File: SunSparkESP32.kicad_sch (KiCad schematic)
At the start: 51 parts, among them J1 Conn_01x02_Pin, J2 USB_C_Receptacle_USB2.0, J3 Conn_01x03_Pin, J4 Conn_01x15_Pin, J5 Conn_01x03_Pin, J6 Conn_01x15_Pin, J7 Conn_01x01_Pin, Q1 IRLML6244TRPBF, Q2 IRLML6244TRPBF, SW1 SW_Push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

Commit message: Rework due to first review -Replaced electrolytic caps with low ESR ceramic ones -Routing optimizations Also added possible connection for backup battery Routed some DIOs from LoRa module on controller Updated outputs and BOM
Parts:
- removed C2, C5: 4.7µ, Capacitor_SMD:CP_Elec_4x3, symbol Device:C_Polarized
- added C2, C5: 4µ7, Capacitor_SMD:C_0805_2012Metric_Pad1.18x1.45mm_HandSolder, symbol Device:C
- added J8: Conn_01x01_Pin, TestPoint:TestPoint_THTPad_D1.5mm_Drill0.7mm, symbol Connector:Conn_01x01_Pin
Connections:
- net GND: now also C2.2, C5.2
- net DIO3: now reaches U4.11 (DIO3)
- net DIO3: now also U3.33 (GPIO37)
- net DIO2: now reaches U4.16 (DIO2)
- net DIO2: now also U3.34 (GPIO38)
- net at J1.1 (Pin_1), L1.1, R2.1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: now also C5.1
- net at JP1.1 (A), TP3.1, U1.11 (SYS): now also C2.1
- net at U1.12 (BACKUP): now also J8.1 (Pin_1)
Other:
- note added: "DIO2/3 used for potential PreambleDetect/SyncAddress"
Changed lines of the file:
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@@
     (stroke (width 0) (type default))
   )
+  (wire (pts (xy 68.58 87.63) (xy 73.66 87.63))
+    (stroke (width 0) (type default))
+  )
   (wire (pts (xy 285.75 163.83) (xy 290.83 163.83))
     (stroke (width 0) (type default))
@@
     (stroke (width 0) (type default))
   )
+  (wire (pts (xy 361.95 116.84) (xy 361.95 113.03))
+    (stroke (width 0) (type default))
+  )
   (wire (pts (xy 212.09 153.67) (xy 212.09 154.94))
     (stroke (width 0) (type default))
@@
     (stroke (width 0) (type default))
   )
+  (wire (pts (xy 360.68 115.57) (xy 355.6 115.57))
+    (stroke (width 0) (type default))
+  )
   (wire (pts (xy 369.57 46.99) (xy 372.11 46.99))
     (stroke (width 0) (type default))
@@
     (stroke (width 0) (type default))
   )
+  (wire (pts (xy 360.68 120.65) (xy 364.49 120.65))
+    (stroke (width 0) (type default))
+  )
   (wire (pts (xy 281.94 41.91) (xy 289.56 41.91))
     (stroke (width 0) (type default))
@@
     (stroke (width 0) (type default))
   )
-  (bus (pts (xy 363.22 119.38) (xy 363.22 113.03))
+  (bus (pts (xy 363.22 113.03) (xy 363.22 110.49))
     (stroke (width 0) (type default))
   )
@@
     (stroke (width 0) (type default))
   )
-  (bus (pts (xy 363.22 110.49) (xy 363.22 113.03))
-    (stroke (width 0) (type default))
-  )
   (wire (pts (xy 129.54 87.63) (xy 129.54 95.25))
     (stroke (width 0) (type default))
@@
     (stroke (width 0) (type default))
   )
+  (wire (pts (xy 361.95 116.84) (xy 364.49 116.84))
+    (stroke (width 0) (type default))
+  )
   (wire (pts (xy 342.9 165.1) (xy 350.52 165.1))
     (stroke (width 0) (type default))
@@
     (stroke (width 0) (type default))
   )
+  (wire (pts (xy 361.95 113.03) (xy 355.6 113.03))
+    (stroke (width 0) (type default))
+  )
   (wire (pts (xy 100.33 39.37) (xy 100.33 43.18))
     (stroke (width 0) (type default))
@@
     (stroke (width 0) (type default))
   )
+  (wire (pts (xy 360.68 120.65) (xy 360.68 115.57))
+    (stroke (width 0) (type default))
+  )
   (wire (pts (xy 281.94 57.15) (xy 289.56 57.15))
     (stroke (width 0) (type default))
@@
     (stroke (width 0) (type default))
   )
+  (wire (pts (xy 236.22 201.93) (xy 242.57 201.93))
+    (stroke (width 0) (type default))
+  )
   (wire (pts (xy 355.6 87.63) (xy 356.87 87.63))
     (stroke (width 0) (type default))
@@
     (stroke (width 0) (type default))
   )
-  (bus (pts (xy 363.22 119.38) (xy 367.03 119.38))
+  (bus (pts (xy 363.22 113.03) (xy 367.03 113.03))
     (stroke (width 0) (type default))
   )
@@
     (stroke (width 0) (type default))
   )
+  (wire (pts (xy 236.22 204.47) (xy 242.57 204.47))
+    (stroke (width 0) (type default))
+  )
   (wire (pts (xy 302.26 166.37) (xy 302.26 163.83))
     (stroke (width 0) (type default))
@@
     (effects (font (size 1.27 1.27)) (justify left bottom))
   )
+  (text "DIO2/3 used for potential\nPreambleDetect/SyncAddress"
+    (at 241.3 199.39 0)
+    (effects (font (size 1.27 1.27)) (justify left bottom))
+  )
   (text "Might also be used to\ninsert shunt for\ncurrent meas."
     (at 78.74 31.75 0)
@@
     (effects (font (size 1.27 1.27)) (justify left bottom))
   )
-  (label "IO[0..4]" (at 367.03 119.38 0) (fields_autoplaced)
+  (label "IO[0..4]" (at 367.03 113.03 0) (fields_autoplaced)
     (effects (font (size 1.27 1.27)) (justify left bottom))
   )
@@
     )
   )
+  (global_label "DIO3" (shape input) (at 242.57 201.93 0) (fields_autoplaced)
+    (effects (font (size 1.27 1.27)) (justify left))
+    (property "Intersheetrefs" "${INTERSHEET_REFS}" (at 249.8906 201.93 0)
+      (effects (font (size 1.27 1.27)) (justify left) hide)
+    )
+  )
   (global_label "AUX_SW_CTRL" (shape input) (at 356.87 80.01 0) (fields_autoplaced)
     (effects (font (size 1.27 1.27)) (justify left))
@@
     )
   )
+  (global_label "DIO2" (shape input) (at 364.49 120.65 0) (fields_autoplaced)
+    (effects (font (size 1.27 1.27)) (justify left))
+    (property "Intersheetrefs" "${INTERSHEET_REFS}" (at 371.8106 120.65 0)
+      (effects (font (size 1.27 1.27)) (justify left) hide)
+    )
+  )
   (global_label "CS0" (shape input) (at 382.27 82.55 180) (fields_autoplaced)
     (effects (font (size 1.27 1.27)) (justify right))
@@
     )
   )
+  (global_label "DIO3" (shape input) (at 364.49 116.84 0) (fields_autoplaced)
+    (effects (font (size 1.27 1.27)) (justify left))
+    (property "Intersheetrefs" "${INTERSHEET_REFS}" (at 371.8106 116.84 0)
+      (effects (font (size 1.27 1.27)) (justify left) hide)
+    )
+  )
+  (global_label "DIO2" (shape input) (at 242.57 204.47 0) (fields_autoplaced)
+    (effects (font (size 1.27 1.27)) (justify left))
+    (property "Intersheetrefs" "${INTERSHEET_REFS}" (at 249.8906 204.47 0)
+      (effects (font (size 1.27 1.27)) (justify left) hide)
+    )
+  )
   (global_label "rst_btn" (shape input) (at 278.13 41.91 180) (fields_autoplaced)
     (effects (font (size 1.27 1.27)) (justify right))
@@
     )
   )
+  (symbol (lib_id "Device:C") (at 78.74 59.69 0) (unit 1)
+    (in_bom yes) (on_board yes) (dnp no) (fields_autoplaced)
+    (property "Reference" "C5" (at 82.55 59.055 0)
+      (effects (font (size 1.27 1.27)) (justify left))
+    )
+    (property "Value" "4µ7" (at 82.55 61.595 0)
+      (effects (font (size 1.27 1.27)) (justify left))
+    )
+    (property "Footprint" "Capacitor_SMD:C_0805_2012Metric_Pad1.18x1.45mm_HandSolder" (at 79.7052 63.5 0)
+      (effects (font (size 1.27 1.27)) hide)
+    )
+    (property "Datasheet" "~" (at 78.74 59.69 0)
+      (effects (font (size 1.27 1.27)) hide)
+    )
+    (pin "1")
+    (pin "2")
+    (instances
+      (project "SunSparkESP32"
+        (path "/d10941bc-74a1-4d19-894b-f93374d839a2"
+          (reference "C5") (unit 1)
+        )
+      )
+    )
+  )
   (symbol (lib_id "Device:C") (at 212.09 149.86 0) (unit 1)
     (in_bom yes) (on_board yes) (dnp no) (fields_autoplaced)
@@
     )
   )
-  (symbol (lib_id "Device:C_Polarized") (at 119.38 80.01 0) (unit 1)
-    (in_bom yes) (on_board yes) (dnp no)
-    (property "Reference" "C5" (at 121.92 80.01 0)
-      (effects (font (size 1.27 1.27)) (justify left))
-    )
-    (property "Value" "4.7µ" (at 120.65 82.55 0)
-      (effects (font (size 1.27 1.27)) (justify left))
-    )
-    (property "Footprint" "Capacitor_SMD:CP_Elec_4x3" (at 120.3452 83.82 0)
-      (effects (font (size 1.27 1.27)) hide)
-    )
-    (property "Datasheet" "~" (at 119.38 80.01 0)
-      (effects (font (size 1.27 1.27)) hide)
-    )
-    (pin "1")
-    (pin "2")
-    (instances
-      (project "SunSparkESP32"
-        (path "/d10941bc-74a1-4d19-894b-f93374d839a2"
-          (reference "C5") (unit 1)
-        )
-      )
-    )
-  )
   (symbol (lib_id "Device:R") (at 85.09 149.86 90) (unit 1)
     (in_bom yes) (on_board yes) (dnp no)
@@
     )
   )
-  (symbol (lib_id "power:+BATT") (at 260.35 34.29 0) (unit 1)
+  (symbol (lib_id "Device:C") (at 119.38 80.01 0) (unit 1)
     (in_bom yes) (on_board yes) (dnp no) (fields_autoplaced)
-    (property "Reference" "#PWR022" (at 260.35 38.1 0)
-      (effects (font (size 1.27 1.27)) hide)
+    (property "Reference" "C2" (at 123.19 79.375 0)
+      (effects (font (size 1.27 1.27)) (justify left))
     )
-    (property "Value" "+BATT" (at 260.35 30.48 0)
-      (effects (font (size 1.27 1.27)))
+    (property "Value" "4µ7" (at 123.19 81.915 0)
+      (effects (font (size 1.27 1.27)) (justify left))
     )
-    (property "Footprint" "" (at 260.35 34.29 0)
+    (property "Footprint" "Capacitor_SMD:C_0805_2012Metric_Pad1.18x1.45mm_HandSolder" (at 120.3452 83.82 0)
       (effects (font (size 1.27 1.27)) hide)
     )
-    (property "Datasheet" "" (at 260.35 34.29 0)
+    (property "Datasheet" "~" (at 119.38 80.01 0)
       (effects (font (size 1.27 1.27)) hide)
     )
     (pin "1")
+    (pin "2")
     (instances
       (project "SunSparkESP32"
         (path "/d10941bc-74a1-4d19-894b-f93374d839a2"
-          (reference "#PWR022") (unit 1)
+          (reference "C2") (unit 1)
         )
       )
     )
   )
-  (symbol (lib_id "Device:C_Polarized") (at 78.74 59.69 0) (unit 1)
-    (in_bom yes) (on_board yes) (dnp no)
-    (property "Reference" "C2" (at 81.28 59.69 0)
-      (effects (font (size 1.27 1.27)) (justify left))
+  (symbol (lib_id "power:+BATT") (at 260.35 34.29 0) (unit 1)
+    (in_bom yes) (on_board yes) (dnp no) (fields_autoplaced)
+    (property "Reference" "#PWR022" (at 260.35 38.1 0)
+      (effects (font (size 1.27 1.27)) hide)
     )
-    (property "Value" "4.7µ" (at 80.01 62.23 0)
-      (effects (font (size 1.27 1.27)) (justify left))
+    (property "Value" "+BATT" (at 260.35 30.48 0)
+      (effects (font (size 1.27 1.27)))
     )
-    (property "Footprint" "Capacitor_SMD:CP_Elec_4x3" (at 79.7052 63.5 0)
+    (property "Footprint" "" (at 260.35 34.29 0)
       (effects (font (size 1.27 1.27)) hide)
     )
-    (property "Datasheet" "~" (at 78.74 59.69 0)
+    (property "Datasheet" "" (at 260.35 34.29 0)
       (effects (font (size 1.27 1.27)) hide)
     )
     (pin "1")
-    (pin "2")
     (instances
       (project "SunSparkESP32"
         (path "/d10941bc-74a1-4d19-894b-f93374d839a2"
-          (reference "C2") (unit 1)
+          (reference "#PWR022") (unit 1)
         )
       )
@@
         )
       )
+    )
+  )
+  (symbol (lib_id "Connector:Conn_01x01_Pin") (at 63.5 87.63 0) (unit 1)
+    (in_bom yes) (on_board yes) (dnp no) (fields_autoplaced)
+    (property "Reference" "J8" (at 64.135 83.82 0)
+      (effects (font (size 1.27 1.27)))
+    )
+    (property "Value" "Conn_01x01_Pin" (at 64.135 86.36 0)
+      (effects (font (size 1.27 1.27)))
+    )
+    (property "Footprint" "TestPoint:TestPoint_THTPad_D1.5mm_Drill0.7mm" (at 63.5 87.63 0)
+      (effects (font (size 1.27 1.27)) hide)
+    )
+    (property "Datasheet" "~" (at 63.5 87.63 0)
+      (effects (font (size 1.27 1.27)) hide)
+    )
+    (pin "1")
+    (instances
+      (project "SunSparkESP32"
+        (path "/d10941bc-74a1-4d19-894b-f93374d839a2"
+          (reference "J8") (unit 1)
+        )
+      )

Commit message: Finalized last review points, enhanced doc -Added Diode to prevent discharge from supercap into LDO -Updated BOM -Made readme nicer
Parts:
- added D1: D_Schottky, Diode_SMD:D_SOD-323, symbol Device:D_Schottky
- added JP2: SolderJumper_2_Open, Jumper:SolderJumper-2_P1.3mm_Open_RoundedPad1.0x1.5mm, symbol Jumper:SolderJumper_2_Open
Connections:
- net at C6.1, U2.2 (VO): now also D1.2 (A), JP2.1 (A); no longer R14.1
- net BCKP: now reaches J8.1 (Pin_1), U1.12 (BACKUP)
- net BCKP: now also JP2.2 (B)
- new net: D1.1 (K), R14.1
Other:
- note added: "Prevent Supercap from discharging through LDO"
- moved on the sheet: J8, R1, R14, R2

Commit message: Added Routing for DIO pins of modem
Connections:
- net DIO4: now reaches U4.12 (DIO4)
- net DIO4: now also J6.13 (Pin_13), U3.7 (GPIO3/ADC1_CH2)
- net DIO0: now reaches U4.14 (DIO0)
- net DIO0: now also J6.14 (Pin_14), U3.6 (GPIO2/ADC1_CH1)
- net DIO1: now reaches U4.15 (DIO1)
- net DIO1: now also U3.41 (GPIO45)
- net DIO5: now reaches U4.7 (DIO5)
- net DIO5: now also J6.12 (Pin_12), U3.8 (GPIO4/ADC1_CH3)
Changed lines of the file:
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@@
+    (effects (font (size 1.27 1.27)) (justify left bottom))
+  )
+  (label "DIO5" (at 236.22 196.85 0) (fields_autoplaced)
     (effects (font (size 1.27 1.27)) (justify left bottom))
   )
@@
     (effects (font (size 1.27 1.27)) (justify left bottom))
   )
+  (label "DIO0" (at 236.22 209.55 0) (fields_autoplaced)
+    (effects (font (size 1.27 1.27)) (justify left bottom))
+  )
   (label "IO0" (at 259.08 67.31 0) (fields_autoplaced)
     (effects (font (size 1.27 1.27)) (justify left bottom))
   )
   (label "IO1" (at 259.08 69.85 0) (fields_autoplaced)
+    (effects (font (size 1.27 1.27)) (justify left bottom))
+  )
+  (label "DIO0" (at 370.84 62.23 0) (fields_autoplaced)
+    (effects (font (size 1.27 1.27)) (justify left bottom))
+  )
+  (label "DIO1" (at 236.22 207.01 0) (fields_autoplaced)
+    (effects (font (size 1.27 1.27)) (justify left bottom))
+  )
+  (label "DIO5" (at 358.14 67.31 0) (fields_autoplaced)
     (effects (font (size 1.27 1.27)) (justify left bottom))
   )
@@
     (effects (font (size 1.27 1.27)) (justify left bottom))
   )
+  (label "DIO1" (at 355.6 118.11 0) (fields_autoplaced)
+    (effects (font (size 1.27 1.27)) (justify left bottom))
+  )
+  (label "DIO4" (at 358.14 64.77 180) (fields_autoplaced)
+    (effects (font (size 1.27 1.27)) (justify right bottom))
+  )
   (label "IO[0..4]" (at 267.97 81.28 0) (fields_autoplaced)
     (effects (font (size 1.27 1.27)) (justify left bottom))
@@
     (effects (font (size 1.27 1.27)) (justify left bottom))
   )
+  (label "DIO4" (at 236.22 199.39 0) (fields_autoplaced)
+    (effects (font (size 1.27 1.27)) (justify left bottom))
+  )

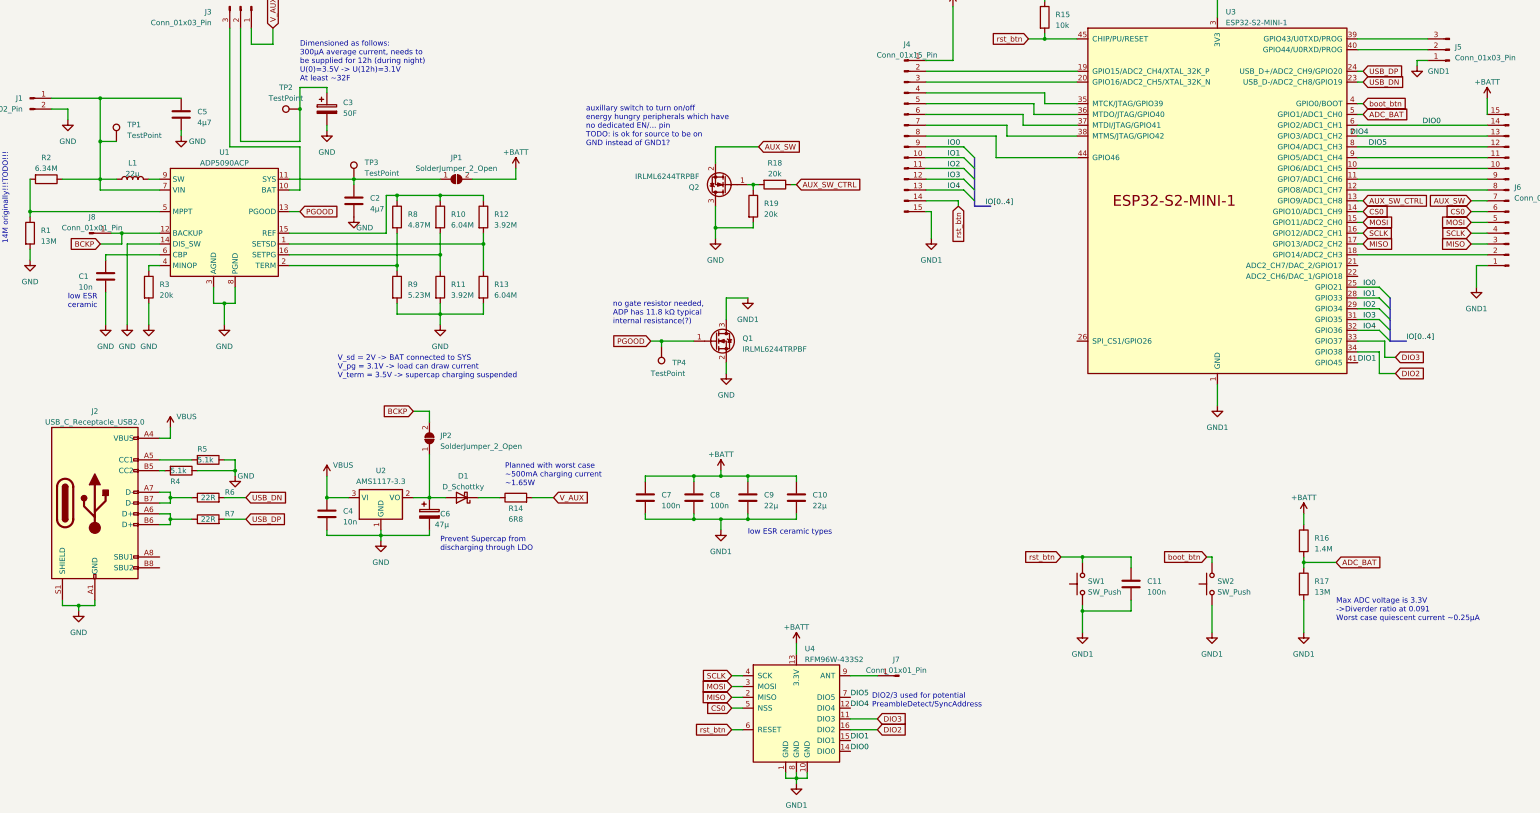
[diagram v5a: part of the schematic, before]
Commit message: Removed some ERC warnings -Added NC flag to non connected pins Remapped some DIOs to actual RTC GPIOs, so that external interrupts in deep sleep are possible
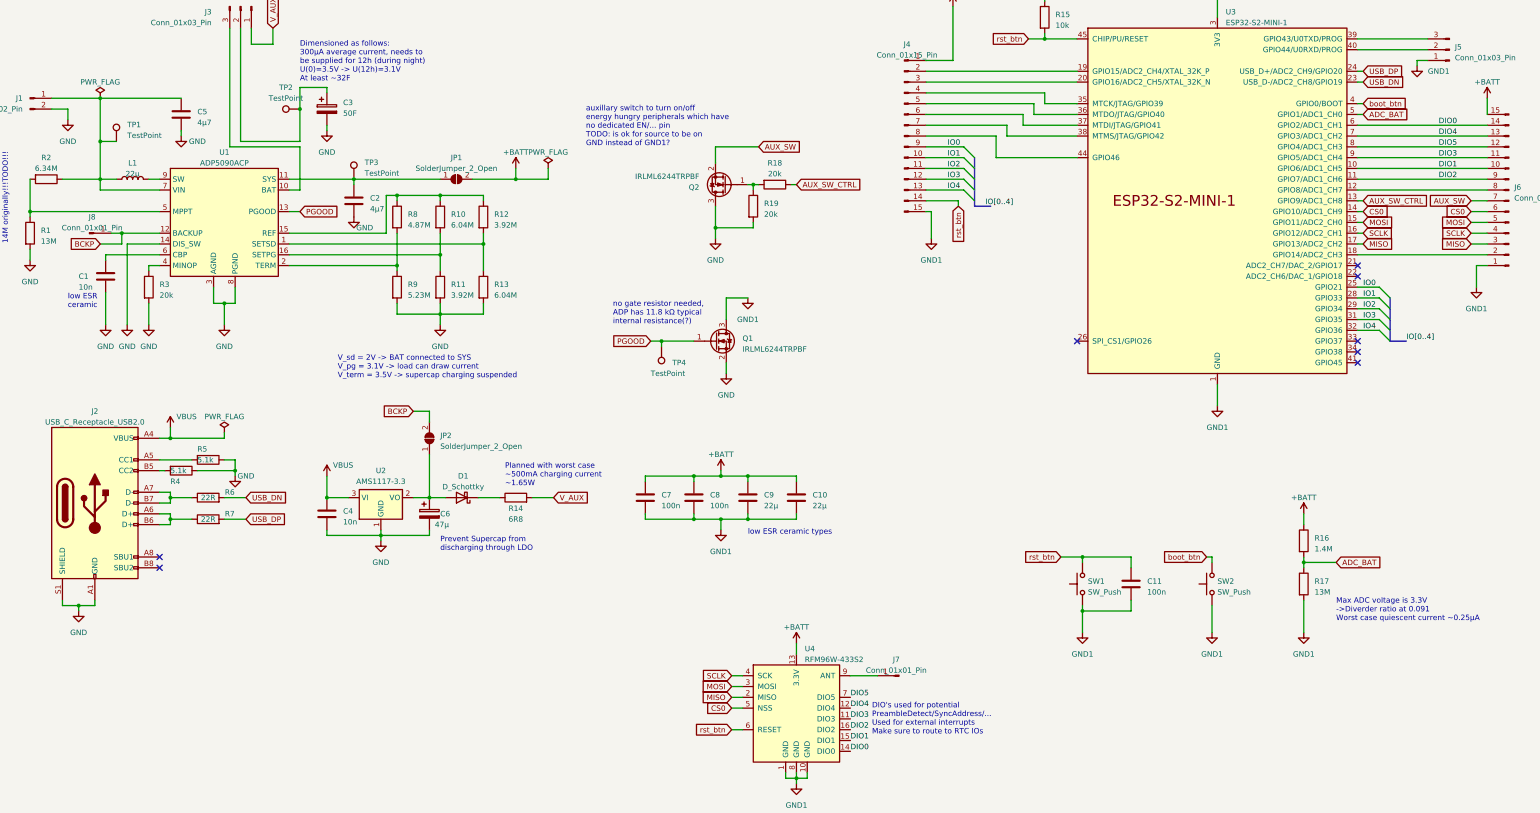
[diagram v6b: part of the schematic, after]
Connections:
- net DIO1: now also J6.10 (Pin_10), U3.10 (GPIO6/ADC1_CH5); no longer U3.41 (GPIO45)
- net DIO2: now also J6.9 (Pin_9), U3.11 (GPIO7/ADC1_CH6); no longer U3.34 (GPIO38)
- net DIO3: now also J6.11 (Pin_11), U3.9 (GPIO5/ADC1_CH4); no longer U3.33 (GPIO37)
- no-connect marks 0 -> 8
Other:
- note added: "DIO's used for potential PreambleDetect/SyncAddress/... Used for external interrupts Make sure to route to RTC IOs"
- note removed: "DIO2/3 used for potential PreambleDetect/SyncAddress"
